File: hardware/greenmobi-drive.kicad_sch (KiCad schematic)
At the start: 33 parts, among them J1 GND, J10 Motor NTC, J2 Encoder/Hall, J3 UBAT, J4 USB_C_Receptacle_USB2.0_14P, J5 CAN, U1 BMI323, U2 TJA1051T-3

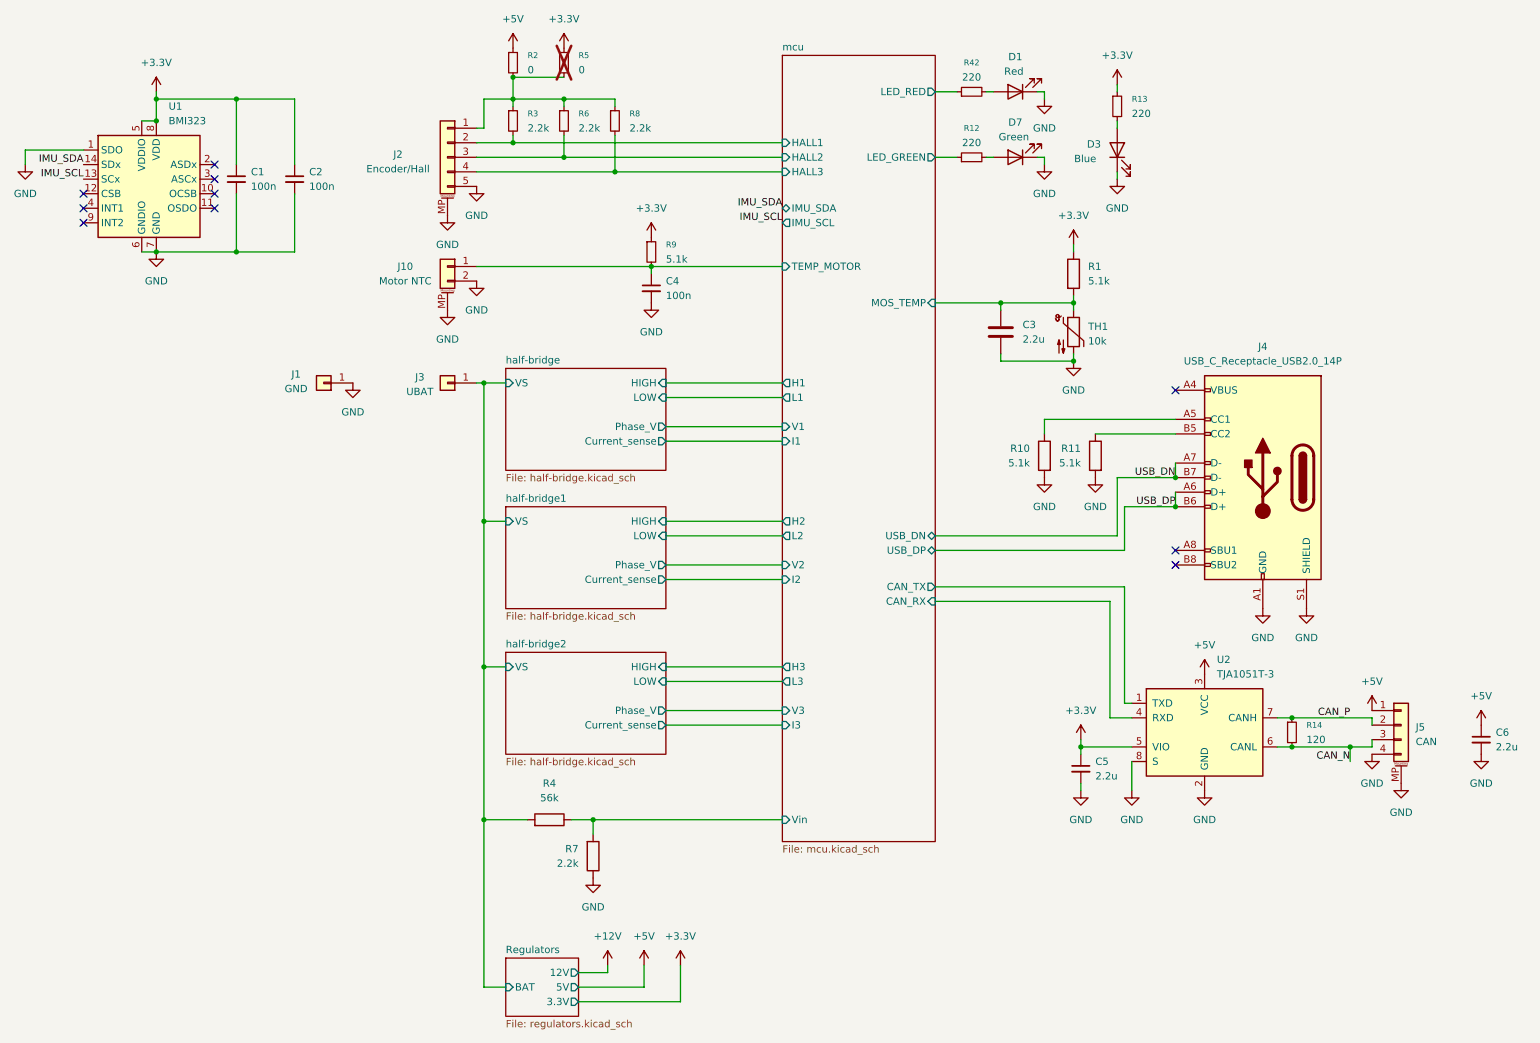
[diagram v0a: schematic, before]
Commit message: TVS and eletrolythic cap
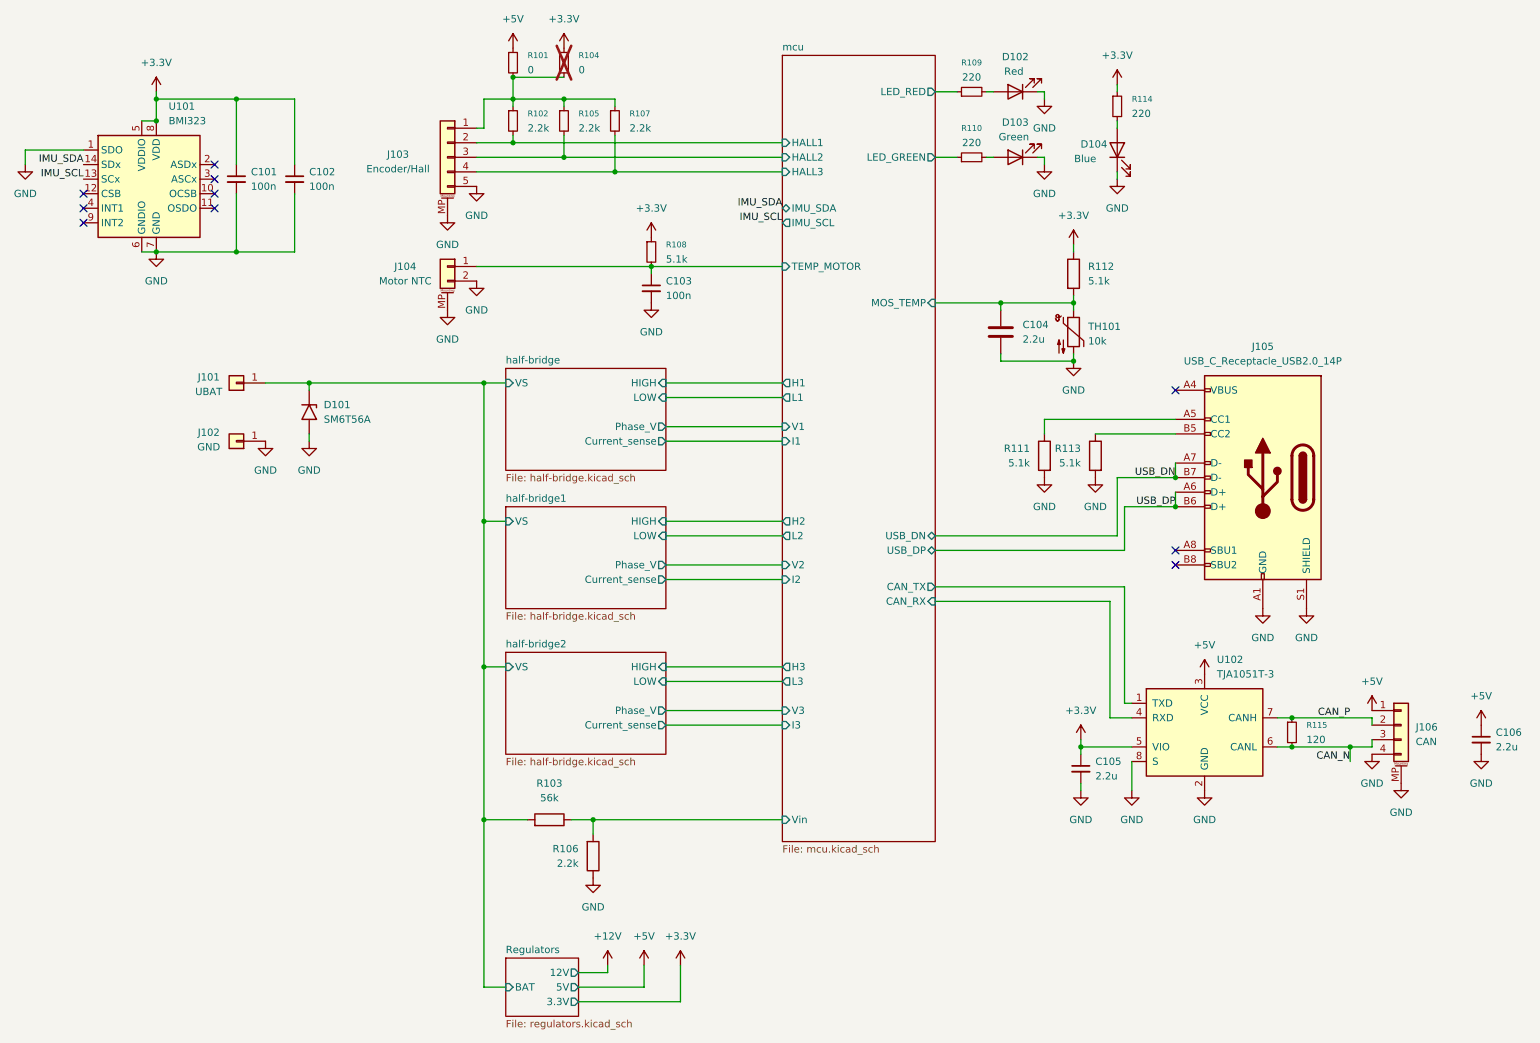
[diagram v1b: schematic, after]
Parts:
- added D101: SM6T56A, Diode_SMD:D_SMB, symbol Diode:SM6T56A
- renumbered C1 to C101, C2 to C102, C4 to C103, C3 to C104, C5 to C105, C6 to C106, D1 to D102, D7 to D103, D3 to D104, J3 to J101, J1 to J102, J2 to J103, J10 to J104, J4 to J105, J5 to J106, R2 to R101, R3 to R102, R4 to R103, R5 to R104, R6 to R105, R7 to R106, R8 to R107, R9 to R108, R42 to R109, R12 to R110, R10 to R111, R1 to R112, R11 to R113, R13 to R114, R14 to R115, TH1 to TH101, U1 to U101, U2 to U102
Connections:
- net GND: now also D101.2 (A2)
- net Regulators/BAT: now also D101.1 (A1)
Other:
- moved on the sheet: J101, J102

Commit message: Change solder wire pads
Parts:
- J101, J102: footprint TestPoint:TestPoint_Pad_4.0x4.0mm -> Connector_Wire:SolderWirePad_1x01_SMD_4x8mm
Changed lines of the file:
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@@
 			)
 		)
-		(property "Footprint" "TestPoint:TestPoint_Pad_4.0x4.0mm"
+		(property "Footprint" "Connector_Wire:SolderWirePad_1x01_SMD_4x8mm"
 			(at 54.61 88.9 0)
 			(effects
@@
 			)
 		)
-		(property "Footprint" "TestPoint:TestPoint_Pad_4.0x4.0mm"
+		(property "Footprint" "Connector_Wire:SolderWirePad_1x01_SMD_4x8mm"
 			(at 54.61 78.74 0)
 			(effects

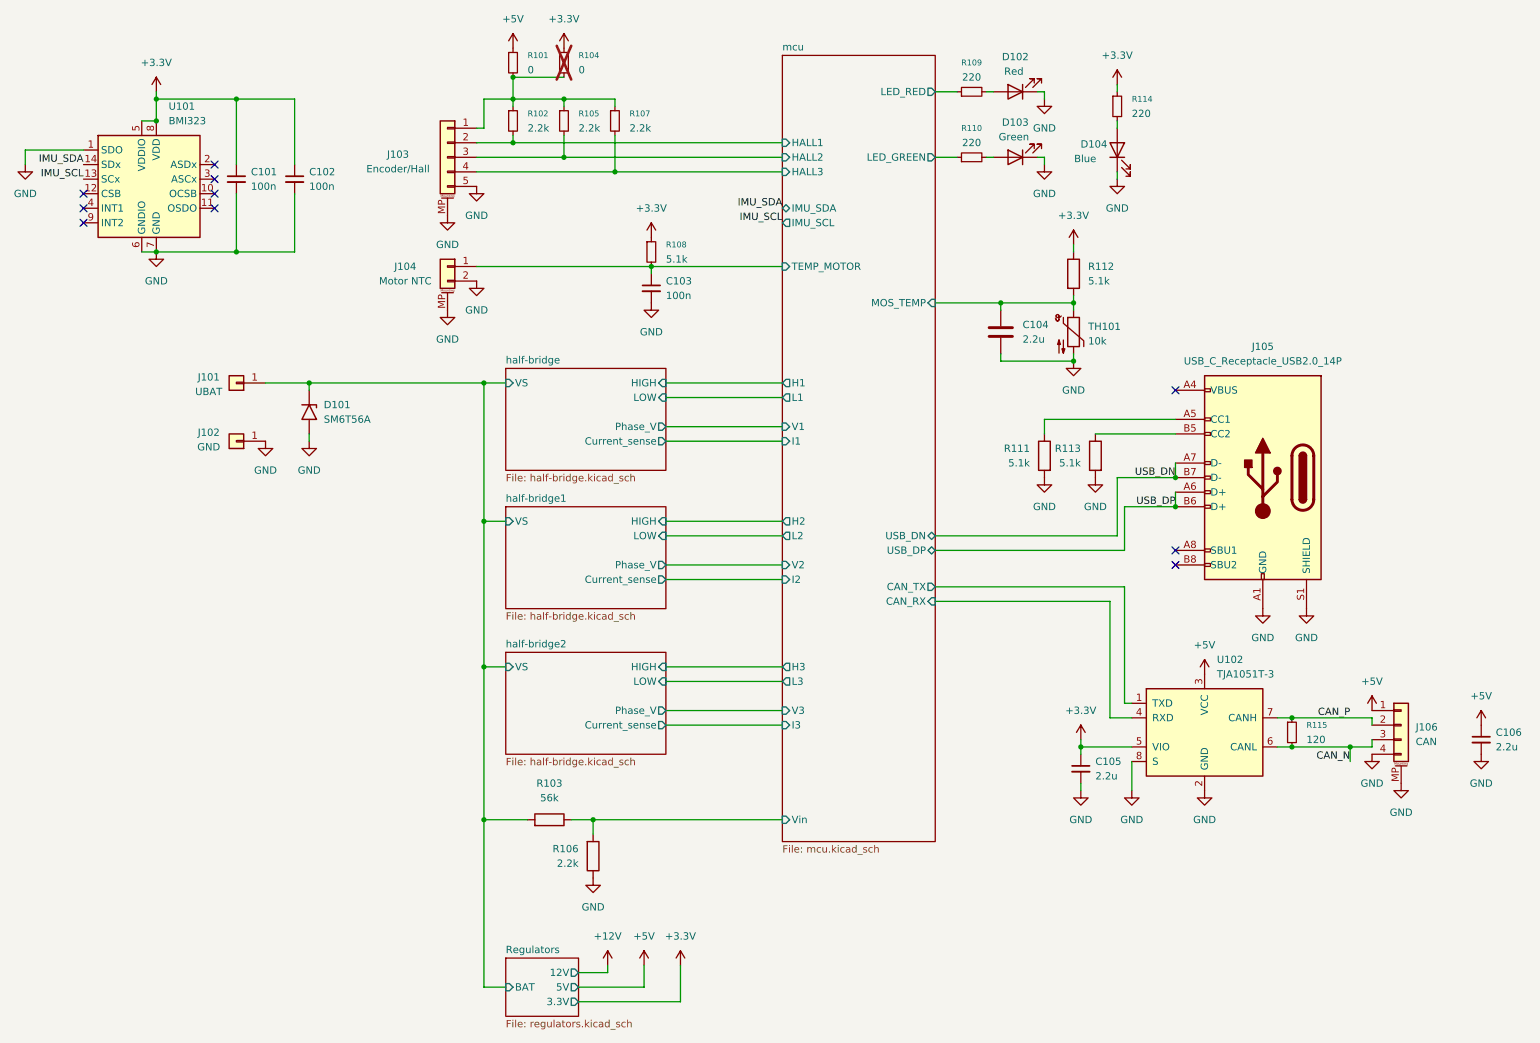
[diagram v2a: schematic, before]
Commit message: Added external analog inputs
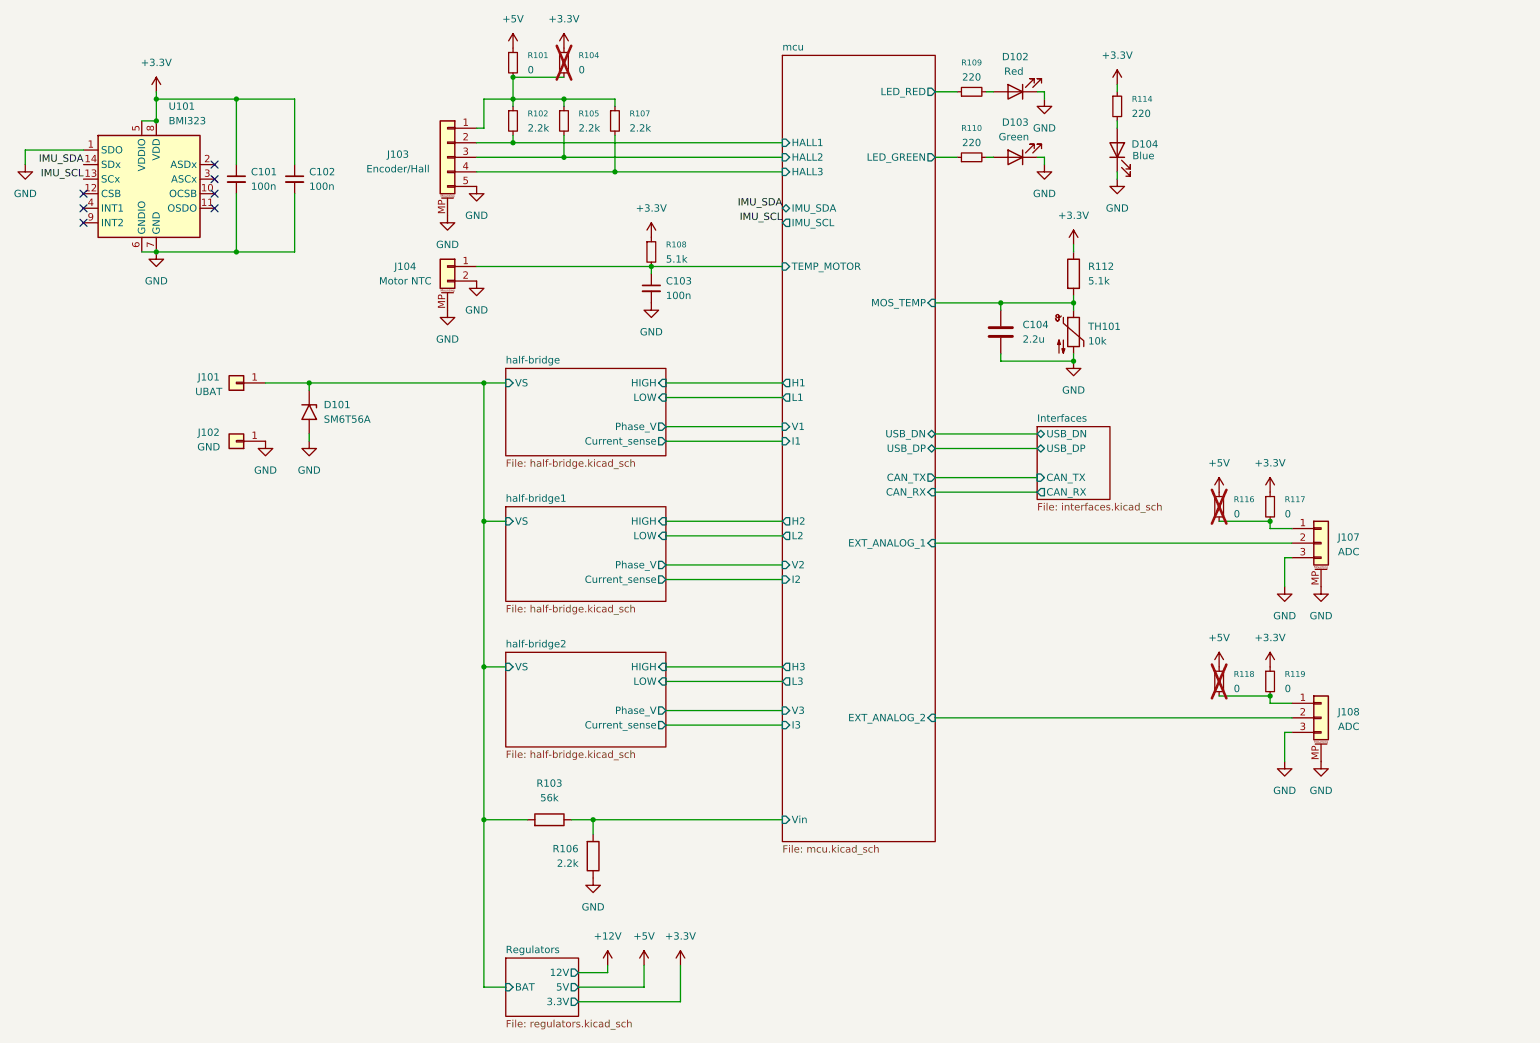
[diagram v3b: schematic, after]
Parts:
- removed C105, C106: 2.2u, Capacitor_SMD:C_0402_1005Metric, symbol Device:C_Small
- removed J105: USB_C_Receptacle_USB2.0_14P, Connector_USB:USB_C_Receptacle_Palconn_UTC16-G, symbol Connector:USB_C_Receptacle_USB2.0_16P
- removed J106: CAN, Connector_JST:JST_GH_SM04B-GHS-TB_1x04-1MP_P1.25mm_Horizontal, symbol Connector_Generic_MountingPin:Conn_01x04_MountingPin
- removed R111, R113: 5.1k, Resistor_SMD:R_0402_1005Metric, symbol Device:R
- removed R115: 120, Resistor_SMD:R_0402_1005Metric, symbol Device:R_Small
- removed U102: TJA1051T-3, Package_SO:SOIC-8_3.9x4.9mm_P1.27mm, symbol Interface_CAN_LIN:TJA1051T-3
- added J107, J108: ADC, Connector_JST:JST_GH_SM03B-GHS-TB_1x03-1MP_P1.25mm_Horizontal, symbol Connector_Generic_MountingPin:Conn_01x03_MountingPin
- added R116, R117, R118, R119: 0, Resistor_SMD:R_0402_1005Metric, symbol Device:R_Small
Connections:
- net +3.3V: now also R117.1, R119.1
- net +5V: now also R116.1, R118.1
- net GND: now also J107.3 (Pin_3), J107.MP (MountPin), J108.3 (Pin_3), J108.MP (MountPin)
- new net: J108.1 (Pin_1), R118.2, R119.2
- new net: J107.1 (Pin_1), R116.2, R117.2
- new net mcu/EXT_ANALOG_1: J107.2 (Pin_2)
- new net mcu/EXT_ANALOG_2: J108.2 (Pin_2)
- no-connect marks 10 -> 7
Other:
- added sheet Interfaces (interfaces.kicad_sch)
- sheet mcu ports: added EXT_ANALOG_1, EXT_ANALOG_2; removed none

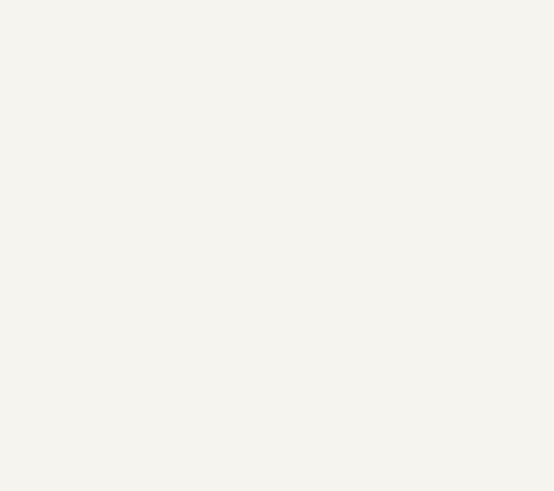
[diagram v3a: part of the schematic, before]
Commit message: Removed buttons for boot and reset
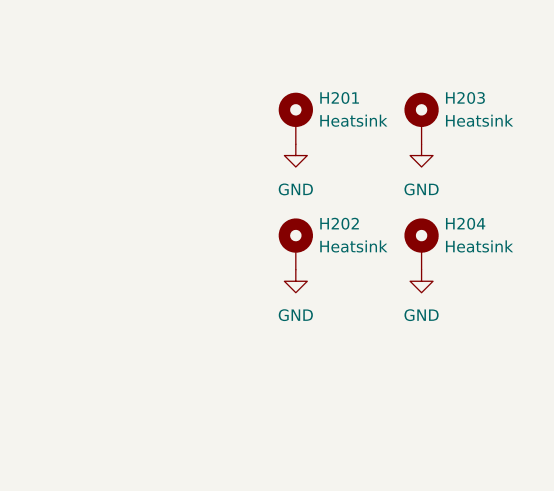
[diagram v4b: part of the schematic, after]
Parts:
- added H201, H202, H203, H204: Heatsink, MountingHole:MountingHole_3.2mm_M3_Pad, symbol Mechanical:MountingHole_Pad
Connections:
- net GND: now also H201.1, H202.1, H203.1, H204.1
